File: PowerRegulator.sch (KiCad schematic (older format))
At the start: 41 parts

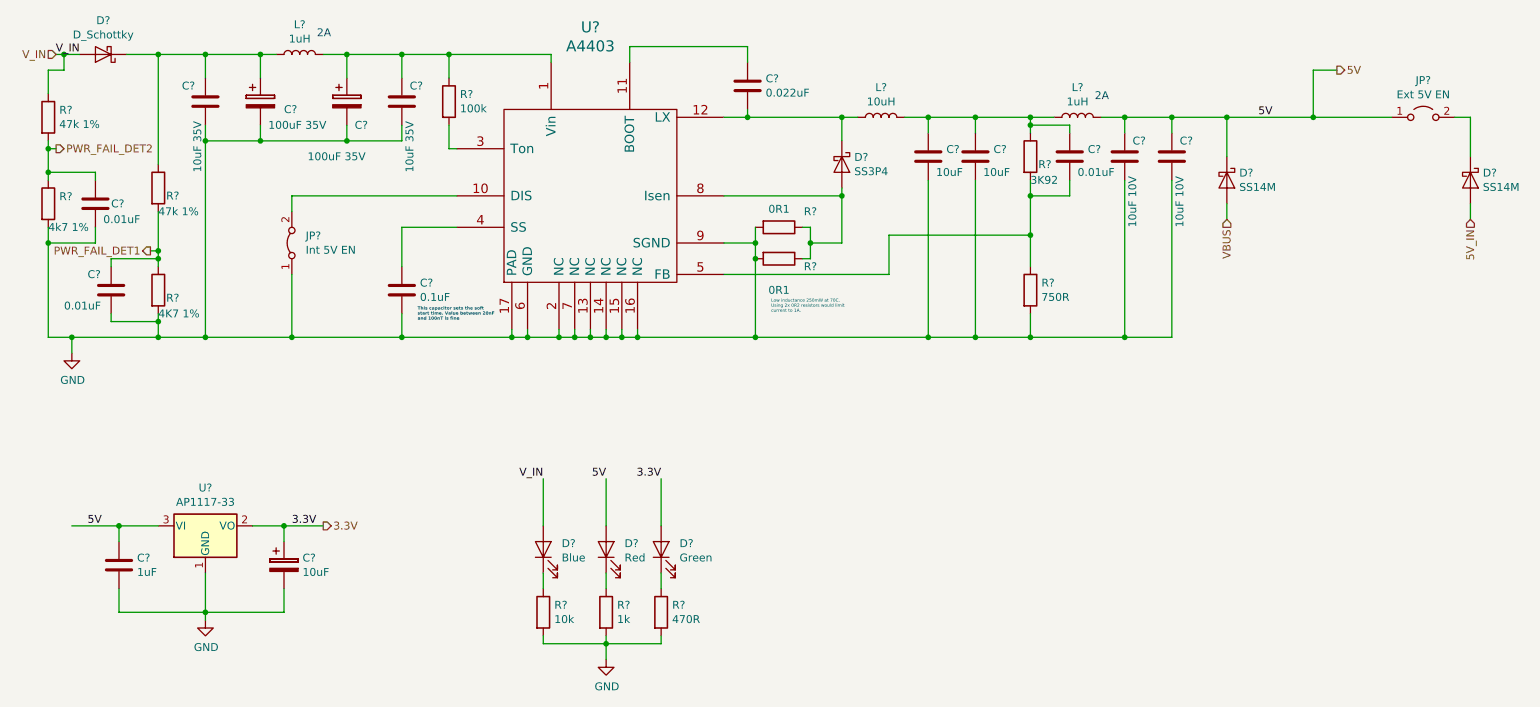
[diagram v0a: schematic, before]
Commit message: Finish the schematics. All pins are assinged to the NUCLEO-64 board.
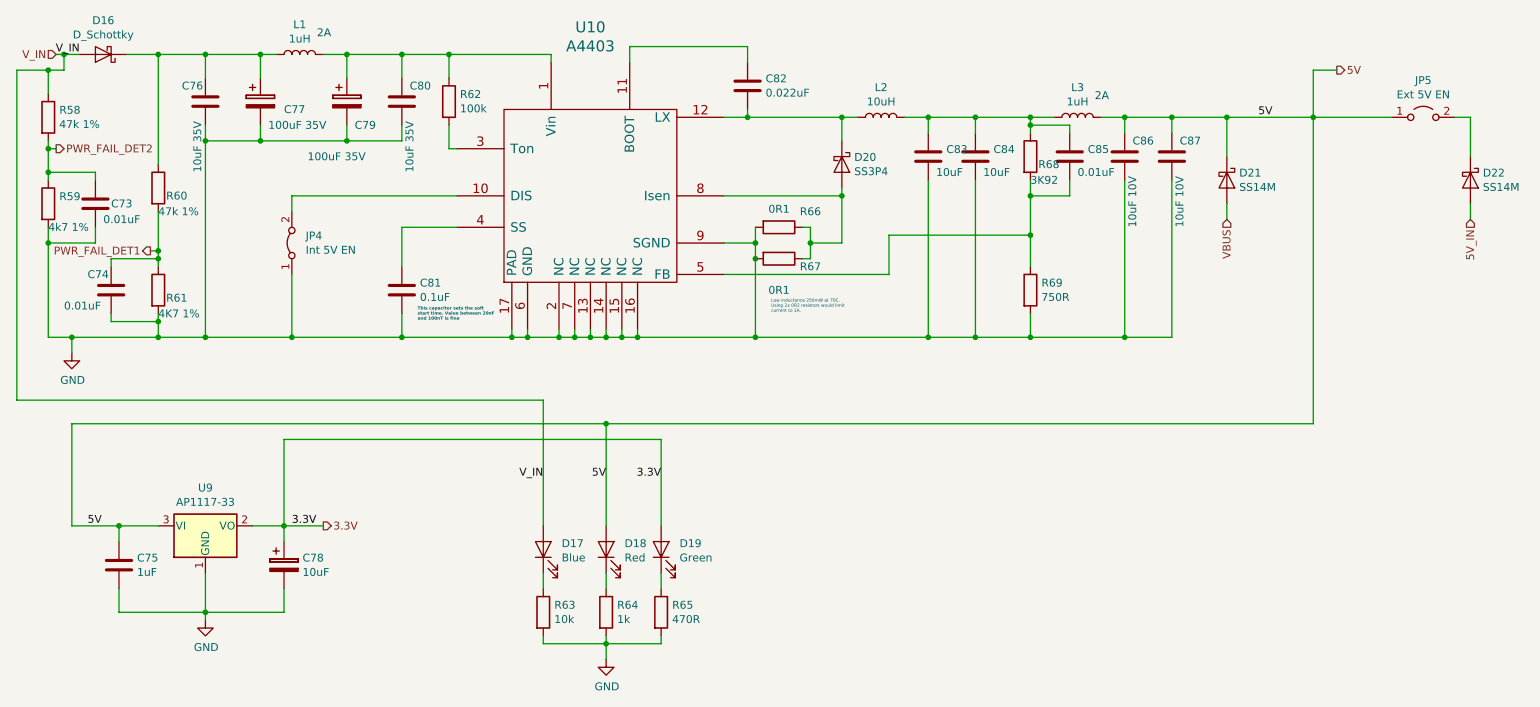
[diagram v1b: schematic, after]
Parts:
- removed U?: AP1117-33, Package_TO_SOT_SMD:SOT-223-3_TabPin2, symbol Regulator_Linear:AP1117-33
- added U9: AP1117-33, Package_TO_SOT_SMD:SOT-223-3_TabPin2, symbol ap1117-15:AP1117-33
- gave numbers to parts that had none: 40
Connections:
- net 3.3V: now also U9.2 (VO)
- net 5V: now also U9.3 (VI)
- net GND: now also U9.1 (GND)

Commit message: Split the bed heater in separate schematics.
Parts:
- D16: value D_Schottky -> SS3P4
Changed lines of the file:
@@
 P 1200 1150
 F 0 "D16" H 1200 934 50  0000 C CNN
-F 1 "D_Schottky" H 1200 1025 50  0000 C CNN
+F 1 "SS3P4" H 1200 1025 50  0000 C CNN
 F 2 "" H 1200 1150 50  0001 C CNN
 F 3 "~" H 1200 1150 50  0001 C CNN

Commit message: Assigned footprints for all components. Inductors are approximate size. MOSFETs dont agree with the footprints. Saved pcb netlist report as report.txt.
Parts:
- C73, C74, C75, C81, C82, C85: footprint (none) -> Capacitor_SMD:C_0603_1608Metric
- C76, C78, C80, C83, C84, C86, C87: footprint (none) -> Capacitor_SMD:CP_Elec_4x5.3
- C77, C79: footprint (none) -> Capacitor_SMD:CP_Elec_6.3x7.7
- D16: footprint (none) -> Diode_SMD:D_SMA
- D17, D18, D19: footprint (none) -> LED_SMD:LED_0603_1608Metric
- D20, D21, D22: footprint (none) -> Diode_SMD:D_SMC
- JP4, JP5: footprint (none) -> Connector_PinHeader_2.54mm:PinHeader_1x02_P2.54mm_Vertical
- L1, L3: footprint (none) -> Inductor_SMD:L_Taiyo-Yuden_MD-4040
- L2: footprint (none) -> Inductor_SMD:L_Sagami_CER1257B
- R58, R59, R60, R61, R62, R63, R64, R65, R68, R69: footprint (none) -> Resistor_SMD:R_0603_1608Metric
- R66, R67: footprint (none) -> Resistor_SMD:R_1206_3216Metric
- U10: footprint (none) -> Package_DFN_QFN:QFN-16-1EP_4x4mm_P0.65mm_EP2.7x2.7mm
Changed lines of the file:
@@
 F 0 "D16" H 1200 934 50  0000 C CNN
 F 1 "SS3P4" H 1200 1025 50  0000 C CNN
-F 2 "" H 1200 1150 50  0001 C CNN
+F 2 "Diode_SMD:D_SMA" H 1200 1150 50  0001 C CNN
 F 3 "~" H 1200 1150 50  0001 C CNN
 	1    1200 1150
@@
 F 0 "R58" H 920 1596 50  0000 L CNN
 F 1 "47k 1%" H 920 1505 50  0000 L CNN
-F 2 "" V 780 1550 50  0001 C CNN
+F 2 "Resistor_SMD:R_0603_1608Metric" V 780 1550 50  0001 C CNN
 F 3 "~" H 850 1550 50  0001 C CNN
 	1    850  1550
@@
 F 0 "R59" H 920 2146 50  0000 L CNN
 F 1 "4k7 1%" H 850 1950 50  0000 L CNN
-F 2 "" V 780 2100 50  0001 C CNN
+F 2 "Resistor_SMD:R_0603_1608Metric" V 780 2100 50  0001 C CNN
 F 3 "~" H 850 2100 50  0001 C CNN
 	1    850  2100
@@
 F 0 "R60" H 1600 1950 50  0000 L CNN
 F 1 "47k 1%" H 1550 1850 50  0000 L CNN
-F 2 "" V 1480 2000 50  0001 C CNN
+F 2 "Resistor_SMD:R_0603_1608Metric" V 1480 2000 50  0001 C CNN
 F 3 "~" H 1550 2000 50  0001 C CNN
 	1    1550 2000
@@
 F 0 "R61" H 1600 2600 50  0000 L CNN
 F 1 "4K7 1%" H 1550 2500 50  0000 L CNN
-F 2 "" V 1480 2650 50  0001 C CNN
+F 2 "Resistor_SMD:R_0603_1608Metric" V 1480 2650 50  0001 C CNN
 F 3 "~" H 1550 2650 50  0001 C CNN
 	1    1550 2650
@@
 F 0 "C73" H 1250 2100 50  0000 L CNN
 F 1 "0.01uF" H 1200 2000 50  0000 L CNN
-F 2 "" H 1188 1950 50  0001 C CNN
+F 2 "Capacitor_SMD:C_0603_1608Metric" H 1188 1950 50  0001 C CNN
 F 3 "~" H 1150 2100 50  0001 C CNN
 	1    1150 2100
@@
 F 0 "C74" H 1100 2750 50  0000 L CNN
 F 1 "0.01uF" H 950 2550 50  0000 L CNN
-F 2 "" H 1288 2500 50  0001 C CNN
+F 2 "Capacitor_SMD:C_0603_1608Metric" H 1288 2500 50  0001 C CNN
 F 3 "~" H 1250 2650 50  0001 C CNN
 	1    1250 2650
@@
 F 0 "C76" H 1700 1550 50  0000 L CNN
 F 1 "10uF 35V" V 1800 1000 50  0000 L CNN
-F 2 "" H 1888 1300 50  0001 C CNN
+F 2 "Capacitor_SMD:CP_Elec_4x5.3" H 1888 1300 50  0001 C CNN
 F 3 "~" H 1850 1450 50  0001 C CNN
 	1    1850 1450
@@
 F 0 "C77" H 2350 1400 50  0000 L CNN
 F 1 "100uF 35V" H 2250 1300 50  0000 L CNN
-F 2 "" H 2238 1300 50  0001 C CNN
+F 2 "Capacitor_SMD:CP_Elec_6.3x7.7" H 2238 1300 50  0001 C CNN
 F 3 "~" H 2200 1450 50  0001 C CNN
 	1    2200 1450
@@
 F 0 "L1" V 2640 1150 50  0000 C CNN
 F 1 "1uH" V 2549 1150 50  0000 C CNN
-F 2 "" H 2450 1150 50  0001 C CNN
+F 2 "Inductor_SMD:L_Taiyo-Yuden_MD-4040" H 2450 1150 50  0001 C CNN
 F 3 "~" H 2450 1150 50  0001 C CNN
 	1    2450 1150
@@
 F 0 "C79" H 2800 1300 50  0000 L CNN
 F 1 "100uF 35V" H 2500 1100 50  0000 L CNN
-F 2 "" H 2788 1300 50  0001 C CNN
+F 2 "Capacitor_SMD:CP_Elec_6.3x7.7" H 2788 1300 50  0001 C CNN
 F 3 "~" H 2750 1450 50  0001 C CNN
 	1    2750 1450
@@
 F 0 "C80" H 3150 1550 50  0000 L CNN
 F 1 "10uF 35V" V 3150 1000 50  0000 L CNN
-F 2 "" H 3138 1300 50  0001 C CNN
+F 2 "Capacitor_SMD:CP_Elec_4x5.3" H 3138 1300 50  0001 C CNN
 F 3 "~" H 3100 1450 50  0001 C CNN
 	1    3100 1450
@@
 F 0 "U10" H 4300 3123 70  0000 C CNN
 F 1 "A4403" H 4300 3002 70  0000 C CNN
-F 2 "" H 4300 2050 60  0000 C CNN
+F 2 "Package_DFN_QFN:QFN-16-1EP_4x4mm_P0.65mm_EP2.7x2.7mm" H 4300 2050 60  0001 C CNN
 F 3 "" H 4300 2050 60  0000 C CNN
 	1    4300 2050
@@
 F 0 "R62" H 3470 1496 50  0000 L CNN
 F 1 "100k" H 3470 1405 50  0000 L CNN
-F 2 "" V 3330 1450 50  0001 C CNN
+F 2 "Resistor_SMD:R_0603_1608Metric" V 3330 1450 50  0001 C CNN
 F 3 "~" H 3400 1450 50  0001 C CNN
 	1    3400 1450
@@
 F 0 "C81" H 3215 2696 50  0000 L CNN
 F 1 "0.1uF" H 3215 2605 50  0000 L CNN
-F 2 "" H 3138 2500 50  0001 C CNN
+F 2 "Capacitor_SMD:C_0603_1608Metric" H 3138 2500 50  0001 C CNN
 F 3 "~" H 3100 2650 50  0001 C CNN
 	1    3100 2650
@@
 F 0 "JP4" V 2446 2262 50  0000 R CNN
 F 1 "Int 5V EN" V 2355 2262 50  0000 R CNN
-F 2 "" H 2400 2350 50  0001 C CNN
+F 2 "Connector_PinHeader_2.54mm:PinHeader_1x02_P2.54mm_Vertical" H 2400 2350 50  0001 C CNN
 F 3 "~" H 2400 2350 50  0001 C CNN
 	1    2400 2350
@@
 F 0 "C82" H 5415 1396 50  0000 L CNN
 F 1 "0.022uF" H 5415 1305 50  0000 L CNN
-F 2 "" H 5338 1200 50  0001 C CNN
+F 2 "Capacitor_SMD:C_0603_1608Metric" H 5338 1200 50  0001 C CNN
 F 3 "~" H 5300 1350 50  0001 C CNN
 	1    5300 1350
@@
 F 0 "R66" V 5400 2450 50  0000 C CNN
 F 1 "0R1" V 5384 2250 50  0000 C CNN
-F 2 "" V 5430 2250 50  0001 C CNN
+F 2 "Resistor_SMD:R_1206_3216Metric" V 5430 2250 50  0001 C CNN
 F 3 "~" H 5500 2250 50  0001 C CNN
 	1    5500 2250
@@
 F 0 "R67" V 5550 2650 50  0000 C CNN
 F 1 "0R1" V 5700 2450 50  0000 C CNN
-F 2 "" V 5430 2450 50  0001 C CNN
+F 2 "Resistor_SMD:R_1206_3216Metric" V 5430 2450 50  0001 C CNN
 F 3 "~" H 5500 2450 50  0001 C CNN
 	1    5500 2450
@@
 F 0 "D20" V 5854 1929 50  0000 L CNN
 F 1 "SS3P4" V 5945 1929 50  0000 L CNN
-F 2 "" H 5900 1850 50  0001 C CNN
+F 2 "Diode_SMD:D_SMC" H 5900 1850 50  0001 C CNN
 F 3 "~" H 5900 1850 50  0001 C CNN
 	1    5900 1850
@@
 F 0 "L2" V 6340 1550 50  0000 C CNN
 F 1 "10uH" V 6249 1550 50  0000 C CNN
-F 2 "" H 6150 1550 50  0001 C CNN
+F 2 "Inductor_SMD:L_Sagami_CER1257B" H 6150 1550 50  0001 C CNN
 F 3 "~" H 6150 1550 50  0001 C CNN
 	1    6150 1550
@@
 F 0 "C83" H 6565 1846 50  0000 L CNN
 F 1 "10uF" H 6500 1700 50  0000 L CNN
-F 2 "" H 6488 1650 50  0001 C CNN
+F 2 "Capacitor_SMD:CP_Elec_4x5.3" H 6488 1650 50  0001 C CNN
 F 3 "~" H 6450 1800 50  0001 C CNN
 	1    6450 1800
@@
 F 0 "C84" H 6865 1846 50  0000 L CNN
 F 1 "10uF" H 6800 1700 50  0000 L CNN
-F 2 "" H 6788 1650 50  0001 C CNN
+F 2 "Capacitor_SMD:CP_Elec_4x5.3" H 6788 1650 50  0001 C CNN
 F 3 "~" H 6750 1800 50  0001 C CNN
 	1    6750 1800
@@
 F 0 "R68" H 7150 1750 50  0000 L CNN
 F 1 "3K92" H 7100 1650 50  0000 L CNN
-F 2 "" V 7030 1800 50  0001 C CNN
+F 2 "Resistor_SMD:R_0603_1608Metric" V 7030 1800 50  0001 C CNN
 F 3 "~" H 7100 1800 50  0001 C CNN
 	1    7100 1800
@@
 F 0 "R69" H 7170 2696 50  0000 L CNN
 F 1 "750R" H 7170 2605 50  0000 L CNN
-F 2 "" V 7030 2650 50  0001 C CNN
+F 2 "Resistor_SMD:R_0603_1608Metric" V 7030 2650 50  0001 C CNN
 F 3 "~" H 7100 2650 50  0001 C CNN
 	1    7100 2650
@@
 F 0 "C85" H 7465 1846 50  0000 L CNN
 F 1 "0.01uF" H 7400 1700 50  0000 L CNN
-F 2 "" H 7388 1650 50  0001 C CNN
+F 2 "Capacitor_SMD:C_0603_1608Metric" H 7388 1650 50  0001 C CNN
 F 3 "~" H 7350 1800 50  0001 C CNN
 	1    7350 1800
@@
 F 0 "L3" V 7590 1550 50  0000 C CNN
 F 1 "1uH" V 7499 1550 50  0000 C CNN
-F 2 "" H 7400 1550 50  0001 C CNN
+F 2 "Inductor_SMD:L_Taiyo-Yuden_MD-4040" H 7400 1550 50  0001 C CNN
 F 3 "~" H 7400 1550 50  0001 C CNN
 	1    7400 1550
@@
 F 0 "C86" H 7750 1900 50  0000 L CNN
 F 1 "10uF 10V" V 7750 1350 50  0000 L CNN
-F 2 "" H 7738 1650 50  0001 C CNN
+F 2 "Capacitor_SMD:CP_Elec_4x5.3" H 7738 1650 50  0001 C CNN
 F 3 "~" H 7700 1800 50  0001 C CNN
 	1    7700 1800
@@
 F 0 "C87" H 8050 1900 50  0000 L CNN
 F 1 "10uF 10V" V 8050 1350 50  0000 L CNN
-F 2 "" H 8038 1650 50  0001 C CNN
+F 2 "Capacitor_SMD:CP_Elec_4x5.3" H 8038 1650 50  0001 C CNN
 F 3 "~" H 8000 1800 50  0001 C CNN
 	1    8000 1800
@@
 F 0 "D21" V 8304 2029 50  0000 L CNN
 F 1 "SS14M" V 8395 2029 50  0000 L CNN
-F 2 "" H 8350 1950 50  0001 C CNN
+F 2 "Diode_SMD:D_SMC" H 8350 1950 50  0001 C CNN
 F 3 "~" H 8350 1950 50  0001 C CNN
 	1    8350 1950
@@
 F 0 "D22" V 9854 2029 50  0000 L CNN
 F 1 "SS14M" V 9945 2029 50  0000 L CNN
-F 2 "" H 9900 1950 50  0001 C CNN
+F 2 "Diode_SMD:D_SMC" H 9900 1950 50  0001 C CNN
 F 3 "~" H 9900 1950 50  0001 C CNN
 	1    9900 1950
@@
 F 0 "JP5" H 9600 1785 50  0000 C CNN
 F 1 "Ext 5V EN" H 9600 1694 50  0000 C CNN
-F 2 "" H 9600 1550 50  0001 C CNN
+F 2 "Connector_PinHeader_2.54mm:PinHeader_1x02_P2.54mm_Vertical" H 9600 1550 50  0001 C CNN
 F 3 "~" H 9600 1550 50  0001 C CNN
 	1    9600 1550
@@
 F 0 "C75" H 1415 4446 50  0000 L CNN
 F 1 "1uF" H 1415 4355 50  0000 L CNN
-F 2 "" H 1338 4250 50  0001 C CNN
+F 2 "Capacitor_SMD:C_0603_1608Metric" H 1338 4250 50  0001 C CNN
 F 3 "~" H 1300 4400 50  0001 C CNN
 	1    1300 4400
@@
 F 0 "C78" H 2468 4446 50  0000 L CNN
 F 1 "10uF" H 2468 4355 50  0000 L CNN
-F 2 "" H 2388 4250 50  0001 C CNN
+F 2 "Capacitor_SMD:CP_Elec_4x5.3" H 2388 4250 50  0001 C CNN
 F 3 "~" H 2350 4400 50  0001 C CNN
 	1    2350 4400
@@
 F 0 "R63" H 4070 4746 50  0000 L CNN
 F 1 "10k" H 4070 4655 50  0000 L CNN
-F 2 "" V 3930 4700 50  0001 C CNN
+F 2 "Resistor_SMD:R_0603_1608Metric" V 3930 4700 50  0001 C CNN
 F 3 "~" H 4000 4700 50  0001 C CNN
 	1    4000 4700
@@
 F 0 "R64" H 4470 4746 50  0000 L CNN
 F 1 "1k" H 4470 4655 50  0000 L CNN
-F 2 "" V 4330 4700 50  0001 C CNN
+F 2 "Resistor_SMD:R_0603_1608Metric" V 4330 4700 50  0001 C CNN
 F 3 "~" H 4400 4700 50  0001 C CNN
 	1    4400 4700
@@
 F 0 "R65" H 4820 4746 50  0000 L CNN
 F 1 "470R" H 4820 4655 50  0000 L CNN
-F 2 "" V 4680 4700 50  0001 C CNN
+F 2 "Resistor_SMD:R_0603_1608Metric" V 4680 4700 50  0001 C CNN
 F 3 "~" H 4750 4700 50  0001 C CNN
 	1    4750 4700
@@
 F 0 "D17" V 4038 4183 50  0000 R CNN
 F 1 "Blue" V 3947 4183 50  0000 R CNN
-F 2 "" H 4000 4300 50  0001 C CNN
+F 2 "LED_SMD:LED_0603_1608Metric" H 4000 4300 50  0001 C CNN
 F 3 "~" H 4000 4300 50  0001 C CNN
 	1    4000 4300
@@
 F 0 "D18" V 4438 4183 50  0000 R CNN
 F 1 "Red" V 4347 4183 50  0000 R CNN
-F 2 "" H 4400 4300 50  0001 C CNN
+F 2 "LED_SMD:LED_0603_1608Metric" H 4400 4300 50  0001 C CNN
 F 3 "~" H 4400 4300 50  0001 C CNN
 	1    4400 4300
@@
 F 0 "D19" V 4788 4183 50  0000 R CNN
 F 1 "Green" V 4697 4183 50  0000 R CNN
-F 2 "" H 4750 4300 50  0001 C CNN
+F 2 "LED_SMD:LED_0603_1608Metric" H 4750 4300 50  0001 C CNN
 F 3 "~" H 4750 4300 50  0001 C CNN
 	1    4750 4300

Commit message: Add missing files from the TMC2130 branch.
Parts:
- C73, C74, C75, C81, C82, C85: footprint Capacitor_SMD:C_0603_1608Metric -> PrntrBoardV1:C_0603_1608Metric
- R58, R59, R60, R61, R62, R63, R64, R65, R68, R69: footprint Resistor_SMD:R_0603_1608Metric -> PrntrBoardV1:R_0603_1608Metric
- R66, R67: footprint Resistor_SMD:R_1206_3216Metric -> PrntrBoardV1:R_1206_3216Metric
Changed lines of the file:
@@
 F 0 "R58" H 920 1596 50  0000 L CNN
 F 1 "47k 1%" H 920 1505 50  0000 L CNN
-F 2 "Resistor_SMD:R_0603_1608Metric" V 780 1550 50  0001 C CNN
+F 2 "PrntrBoardV1:R_0603_1608Metric" V 780 1550 50  0001 C CNN
 F 3 "~" H 850 1550 50  0001 C CNN
 	1    850  1550
@@
 F 0 "R59" H 920 2146 50  0000 L CNN
 F 1 "4k7 1%" H 850 1950 50  0000 L CNN
-F 2 "Resistor_SMD:R_0603_1608Metric" V 780 2100 50  0001 C CNN
+F 2 "PrntrBoardV1:R_0603_1608Metric" V 780 2100 50  0001 C CNN
 F 3 "~" H 850 2100 50  0001 C CNN
 	1    850  2100
@@
 F 0 "R60" H 1600 1950 50  0000 L CNN
 F 1 "47k 1%" H 1550 1850 50  0000 L CNN
-F 2 "Resistor_SMD:R_0603_1608Metric" V 1480 2000 50  0001 C CNN
+F 2 "PrntrBoardV1:R_0603_1608Metric" V 1480 2000 50  0001 C CNN
 F 3 "~" H 1550 2000 50  0001 C CNN
 	1    1550 2000
@@
 F 0 "R61" H 1600 2600 50  0000 L CNN
 F 1 "4K7 1%" H 1550 2500 50  0000 L CNN
-F 2 "Resistor_SMD:R_0603_1608Metric" V 1480 2650 50  0001 C CNN
+F 2 "PrntrBoardV1:R_0603_1608Metric" V 1480 2650 50  0001 C CNN
 F 3 "~" H 1550 2650 50  0001 C CNN
 	1    1550 2650
@@
 F 0 "C73" H 1250 2100 50  0000 L CNN
 F 1 "0.01uF" H 1200 2000 50  0000 L CNN
-F 2 "Capacitor_SMD:C_0603_1608Metric" H 1188 1950 50  0001 C CNN
+F 2 "PrntrBoardV1:C_0603_1608Metric" H 1188 1950 50  0001 C CNN
 F 3 "~" H 1150 2100 50  0001 C CNN
 	1    1150 2100
@@
 F 0 "C74" H 1100 2750 50  0000 L CNN
 F 1 "0.01uF" H 950 2550 50  0000 L CNN
-F 2 "Capacitor_SMD:C_0603_1608Metric" H 1288 2500 50  0001 C CNN
+F 2 "PrntrBoardV1:C_0603_1608Metric" H 1288 2500 50  0001 C CNN
 F 3 "~" H 1250 2650 50  0001 C CNN
 	1    1250 2650
@@
 F 0 "R62" H 3470 1496 50  0000 L CNN
 F 1 "100k" H 3470 1405 50  0000 L CNN
-F 2 "Resistor_SMD:R_0603_1608Metric" V 3330 1450 50  0001 C CNN
+F 2 "PrntrBoardV1:R_0603_1608Metric" V 3330 1450 50  0001 C CNN
 F 3 "~" H 3400 1450 50  0001 C CNN
 	1    3400 1450
@@
 F 0 "C81" H 3215 2696 50  0000 L CNN
 F 1 "0.1uF" H 3215 2605 50  0000 L CNN
-F 2 "Capacitor_SMD:C_0603_1608Metric" H 3138 2500 50  0001 C CNN
+F 2 "PrntrBoardV1:C_0603_1608Metric" H 3138 2500 50  0001 C CNN
 F 3 "~" H 3100 2650 50  0001 C CNN
 	1    3100 2650
@@
 F 0 "C82" H 5415 1396 50  0000 L CNN
 F 1 "0.022uF" H 5415 1305 50  0000 L CNN
-F 2 "Capacitor_SMD:C_0603_1608Metric" H 5338 1200 50  0001 C CNN
+F 2 "PrntrBoardV1:C_0603_1608Metric" H 5338 1200 50  0001 C CNN
 F 3 "~" H 5300 1350 50  0001 C CNN
 	1    5300 1350
@@
 F 0 "R66" V 5400 2450 50  0000 C CNN
 F 1 "0R1" V 5384 2250 50  0000 C CNN
-F 2 "Resistor_SMD:R_1206_3216Metric" V 5430 2250 50  0001 C CNN
+F 2 "PrntrBoardV1:R_1206_3216Metric" V 5430 2250 50  0001 C CNN
 F 3 "~" H 5500 2250 50  0001 C CNN
 	1    5500 2250
@@
 F 0 "R67" V 5550 2650 50  0000 C CNN
 F 1 "0R1" V 5700 2450 50  0000 C CNN
-F 2 "Resistor_SMD:R_1206_3216Metric" V 5430 2450 50  0001 C CNN
+F 2 "PrntrBoardV1:R_1206_3216Metric" V 5430 2450 50  0001 C CNN
 F 3 "~" H 5500 2450 50  0001 C CNN
 	1    5500 2450
@@
 F 0 "R68" H 7150 1750 50  0000 L CNN
 F 1 "3K92" H 7100 1650 50  0000 L CNN
-F 2 "Resistor_SMD:R_0603_1608Metric" V 7030 1800 50  0001 C CNN
+F 2 "PrntrBoardV1:R_0603_1608Metric" V 7030 1800 50  0001 C CNN
 F 3 "~" H 7100 1800 50  0001 C CNN
 	1    7100 1800
@@
 F 0 "R69" H 7170 2696 50  0000 L CNN
 F 1 "750R" H 7170 2605 50  0000 L CNN
-F 2 "Resistor_SMD:R_0603_1608Metric" V 7030 2650 50  0001 C CNN
+F 2 "PrntrBoardV1:R_0603_1608Metric" V 7030 2650 50  0001 C CNN
 F 3 "~" H 7100 2650 50  0001 C CNN
 	1    7100 2650
@@
 F 0 "C85" H 7465 1846 50  0000 L CNN
 F 1 "0.01uF" H 7400 1700 50  0000 L CNN
-F 2 "Capacitor_SMD:C_0603_1608Metric" H 7388 1650 50  0001 C CNN
+F 2 "PrntrBoardV1:C_0603_1608Metric" H 7388 1650 50  0001 C CNN
 F 3 "~" H 7350 1800 50  0001 C CNN
 	1    7350 1800
@@
 F 0 "C75" H 1415 4446 50  0000 L CNN
 F 1 "1uF" H 1415 4355 50  0000 L CNN
-F 2 "Capacitor_SMD:C_0603_1608Metric" H 1338 4250 50  0001 C CNN
+F 2 "PrntrBoardV1:C_0603_1608Metric" H 1338 4250 50  0001 C CNN
 F 3 "~" H 1300 4400 50  0001 C CNN
 	1    1300 4400
@@
 F 0 "R63" H 4070 4746 50  0000 L CNN
 F 1 "10k" H 4070 4655 50  0000 L CNN
-F 2 "Resistor_SMD:R_0603_1608Metric" V 3930 4700 50  0001 C CNN
+F 2 "PrntrBoardV1:R_0603_1608Metric" V 3930 4700 50  0001 C CNN
 F 3 "~" H 4000 4700 50  0001 C CNN
 	1    4000 4700
@@
 F 0 "R64" H 4470 4746 50  0000 L CNN
 F 1 "1k" H 4470 4655 50  0000 L CNN
-F 2 "Resistor_SMD:R_0603_1608Metric" V 4330 4700 50  0001 C CNN
+F 2 "PrntrBoardV1:R_0603_1608Metric" V 4330 4700 50  0001 C CNN
 F 3 "~" H 4400 4700 50  0001 C CNN
 	1    4400 4700
@@
 F 0 "R65" H 4820 4746 50  0000 L CNN
 F 1 "470R" H 4820 4655 50  0000 L CNN
-F 2 "Resistor_SMD:R_0603_1608Metric" V 4680 4700 50  0001 C CNN
+F 2 "PrntrBoardV1:R_0603_1608Metric" V 4680 4700 50  0001 C CNN
 F 3 "~" H 4750 4700 50  0001 C CNN
 	1    4750 4700
